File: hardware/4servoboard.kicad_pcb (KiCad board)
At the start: 2 copper layers, 22.9 x 23.6 mm, 34 parts, among them J1 USB_C_Receptacle, J2 PWM, J3 UART, J4 GND, J5 V_SERVO, J6 POWER, J7 DEBUG, U1 CH32X035F7P6, U2 XC6206P332MR

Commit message: wip: Rev0.4への更新
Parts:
- removed D1: SERVO_PWR, LED_SMD:LED_0603_1608Metric_Pad1.05x0.95mm_HandSolder
- removed QR*****: qr-uart-fscb, qr:qr-uart-fscb
- removed R11: 5.1k, Resistor_SMD:R_0603_1608Metric_Pad0.98x0.95mm_HandSolder
- removed R5: 1k, Resistor_SMD:R_0603_1608Metric_Pad0.98x0.95mm_HandSolder
- added D3: MCU_LED2, LED_SMD:LED_0603_1608Metric_Pad1.05x0.95mm_HandSolder, F.Cu at (127.9, 57.0)
- added J8: DEBUG, Connector_PinHeader_2.54mm:PinHeader_1x02_P2.54mm_Vertical, F.Cu at (127.4, 59.5)
- added R17: 5k1, Resistor_SMD:R_0603_1608Metric_Pad0.98x0.95mm_HandSolder, F.Cu at (115.7, 59.4)
- added REF**: MountingHole_2.2mm_M2_DIN965_Pad, MountingHole:MountingHole_2.2mm_M2_DIN965_Pad, F.Cu at (122.3, 54.4)
- added REF**: MountingHole_2.2mm_M2_DIN965_Pad, MountingHole:MountingHole_2.2mm_M2_DIN965_Pad, F.Cu at (130.7, 54.4)
- D2: value MCU_LED -> MCU_LED1
- J1: footprint PCM_SparkFun-Connector:USB-C_16 -> Download_Lib:USB-C_16-HandSolder
- J6: value POWER -> VBUS; footprint Connector_PinHeader_2.54mm:PinHeader_1x04_P2.54mm_Vertical -> Connector_PinHeader_2.54mm:PinHeader_1x02_P2.54mm_Vertical
- J7: value DEBUG -> GND; footprint Connector_PinHeader_1.27mm:PinHeader_1x02_P1.27mm_Vertical -> Connector_PinHeader_2.54mm:PinHeader_1x02_P2.54mm_Vertical
- R10: value 120k -> 1k
- R12, R13: value 1k -> 5k1
- R14, R8: value 5.1k -> 5k1
- R15, R16: value 1k -> 22
- TH1: value Thermistor_NTC -> 22k/B4050/NTC; footprint Resistor_SMD:R_0603_1608Metric_Pad0.98x0.95mm_HandSolder -> PCM_Resistor_SMD_AKL:R_0603_1608Metric_Pad0.98x0.95mm_HandSolder
- U2: footprint Package_TO_SOT_SMD:SOT-23_Handsoldering -> Package_TO_SOT_SMD:SOT-23
- moved D2 111.6 mm to (116.7, 57.0), turned to 0 degrees
- moved R15 108.7 mm to (117.4, 59.4), turned to -90 degrees
- moved R13 106.2 mm to (118.9, 59.4), turned to 90 degrees
- moved R8 106.0 mm to (115.7, 62.7), turned to 90 degrees
- moved R7 106.0 mm to (115.7, 66.0), turned to 90 degrees
- moved C2 105.8 mm to (119.8, 72.3), turned to 180 degrees
- moved R12 104.8 mm to (120.4, 59.4), turned to 90 degrees
- moved R16 104.0 mm to (121.9, 59.4), turned to -90 degrees
- moved R4 102.8 mm to (115.9, 73.0), turned to 90 degrees
- moved JP1 102.8 mm to (118.1, 60.0), turned to 180 degrees
- moved U2 102.6 mm to (119.5, 69.9), turned to 180 degrees
- moved R3 101.5 mm to (117.3, 73.0), turned to 90 degrees
- moved R14 100.1 mm to (116.8, 69.6)
- moved J7 99.9 mm to (128.8, 73.2)
- moved R6 99.7 mm to (120.0, 57.0)
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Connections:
- net PWM2 renamed PWM2/ADC2
- J2 pad 1: PWM0 -> PWM0/ADC0
- J2 pad 2: PWM1 -> PWM1/ADC1
- J2 pad 4: PWM3 -> PWM3/ADC3
- J6 pad 2: GND -> VBUS
- J7 pad 1: SWCLK -> GND
- J7 pad 2: SWDIO -> GND
- JP1 pad 1: DP -> Net-(JP1-A)
- R10 pad 1: OPA_O -> VDD
- R10 pad 2: OPA_N -> Net-(D3-K)
- R14 pad 2: PC3 -> TEMP_SENCE
- R15 pad 2: TX2 -> UART_B
- R16 pad 2: TX4 -> UART_A
- R6 pad 2: MCU_LED -> MCU_LED1
- R7 pad 2: PB1 -> V_SENCE
- R8 pad 1: PB1 -> V_SENCE
- TH1 pad 1: PC3 -> TEMP_SENCE
- U1 pad 1: PWM0 -> MCU_LED1
- U1 pad 10: OPA_O -> unconnected-(U1-PA4-Pad10)
- U1 pad 11: TX4 -> UART_B
- U1 pad 12: MCU_LED -> V_SENCE
- U1 pad 14: PB1 -> TEMP_SENCE
- U1 pad 4: PC3 -> MCU_LED2
- U1 pad 5: PWM1 -> PWM3/ADC3
- U1 pad 7: OPA_N -> PWM1/ADC1
- U1 pad 8: TX2 -> UART_A
- U1 pad 9: PWM3 -> PWM0/ADC0
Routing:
- net GND: track 154.2 -> 28.4 mm, vias 17 -> 24
- net VBUS: track 119.0 -> 22.5 mm, vias 10 -> 5
- net PC3: track 22.8 -> 0.00 mm, vias 2 -> 0
- net CC1: track 37.3 -> 15.1 mm, vias 3 -> 0
- net TEMP_SENCE: track 0.00 -> 19.7 mm, vias 0 -> 4
- net Net-(J1-D--PadA7): track 28.5 -> 12.6 mm
- net MCU_LED: track 15.9 -> 0.00 mm, vias 2 -> 0
- net PWM3: track 15.9 -> 0.00 mm, vias 1 -> 0
- net PWM1: track 15.7 -> 0.00 mm, vias 1 -> 0
- net Net-(J1-D+-PadA6): track 27.4 -> 11.8 mm
- net TX2: track 15.3 -> 0.00 mm, vias 4 -> 0
- net PWM2/ADC2: track 20.3 -> 5.26 mm, vias 1 -> 0
- net MCU_LED2: track 0.00 -> 14.4 mm, vias 0 -> 2
- net PB1: track 14.2 -> 0.00 mm, vias 2 -> 0
- net TX4: track 13.5 -> 0.00 mm, vias 2 -> 0
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- added copper zone on B.Cu, net OPA_P
- added copper zone on F.Cu, net OPA_P
- added copper zone on B.Cu, net VBUS
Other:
- board size 22.9 x 23.6 mm -> 18.7 x 32.9 mm
- board text removed: "DLM(4.7k)"
- board text removed: "GND"
- board text removed: "Made by EsEhEhElp"
- board text removed: "PWM"
- board text removed: "SWCLK"
- board text removed: "SWDIO"
- board text removed: "UART-FSCB V0.3"
- board text removed: "UART0"
- board text removed: "UART1"
- board text removed: "VBUS"

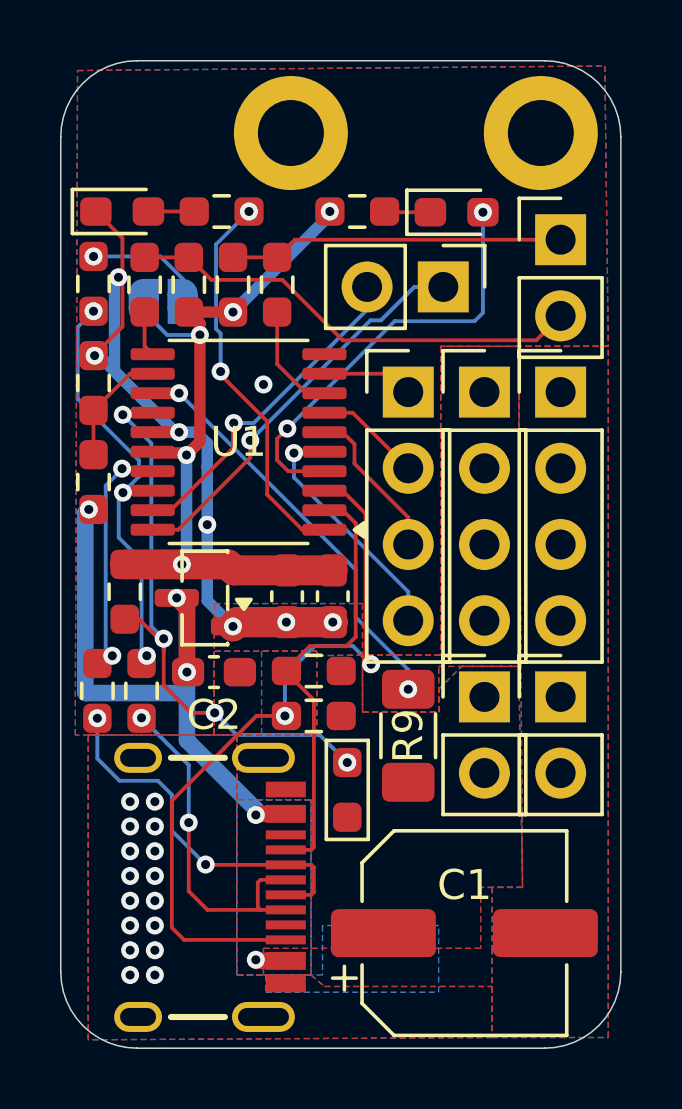
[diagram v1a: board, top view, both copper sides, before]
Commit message: feat: V0.4移行、電源回路の強化
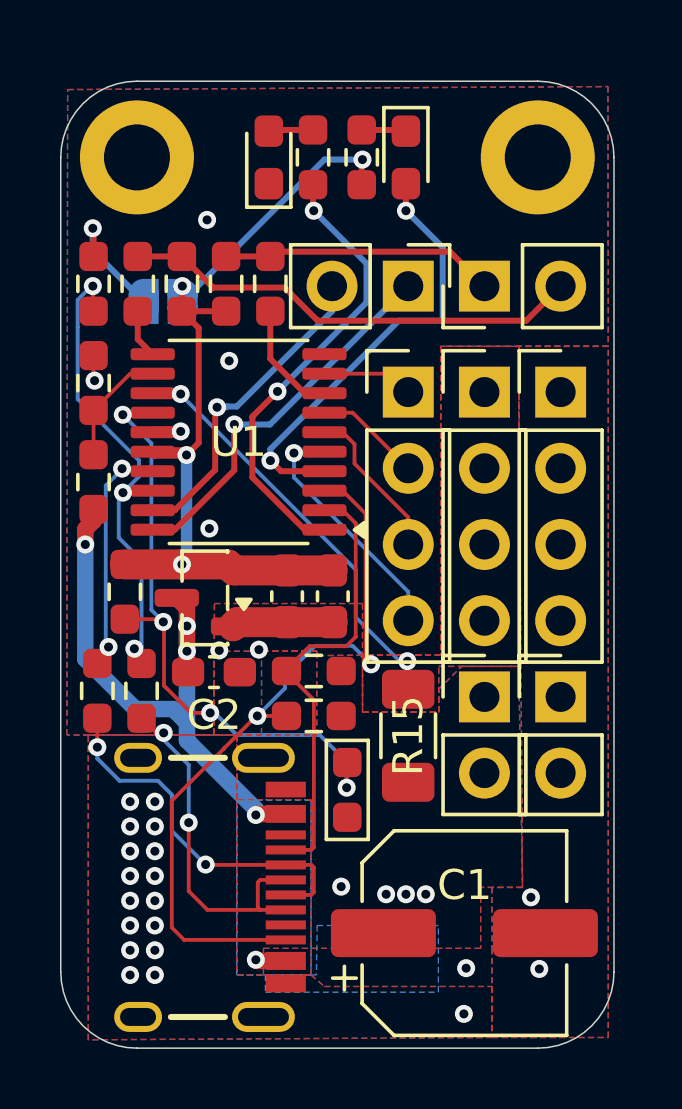
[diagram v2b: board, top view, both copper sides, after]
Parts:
- removed R16: 22, Resistor_SMD:R_0603_1608Metric_Pad0.98x0.95mm_HandSolder
- removed R17: 5k1, Resistor_SMD:R_0603_1608Metric_Pad0.98x0.95mm_HandSolder
- added R12: 22, Resistor_SMD:R_0603_1608Metric_Pad0.98x0.95mm_HandSolder, F.Cu at (121.6, 59.4)
- added R9: 5k1, Resistor_SMD:R_0603_1608Metric_Pad0.98x0.95mm_HandSolder, F.Cu at (115.7, 59.4)
- moved D2 5.21 mm to (121.6, 55.2), turned to 90 degrees
- moved REF2 5.20 mm to (117.2, 55.2)
- moved R5 3.54 mm to (123.1, 55.2), turned to -90 degrees
- moved J3 2.98 mm to (128.8, 59.5), turned to 90 degrees
- moved D3 2.49 mm to (126.2, 55.2), turned to -90 degrees
- moved R6 1.81 mm to (124.7, 55.2), turned to 90 degrees
- moved J8 1.17 mm to (126.2, 59.5)
- moved REF1 0.82 mm to (130.6, 55.2)
- moved R11 0.23 mm to (117.2, 59.4)
- moved R13 0.23 mm to (120.2, 59.4)
- moved R14 0.23 mm to (118.7, 59.4)
- turned JP1 to 0 degrees
- renumbered R14 to R10, R15 to R11, R12 to R13, R13 to R14, R9 to R15, R6 to R5, R10 to R6, REF** to REF1, REF** to REF2
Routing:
- net GND: track 28.4 -> 5.28 mm, vias 24 -> 28
- net VDD: track 25.7 -> 28.7 mm, vias 5 -> 4
- net MCU_LED1: track 13.0 -> 15.2 mm
- net Net-(J3-Pin_1): track 11.2 -> 9.15 mm
- net DP: track 14.2 -> 15.8 mm
- net VBUS: track 22.5 -> 21.3 mm, vias 5 -> 8
- net TEMP_SENCE: track 19.7 -> 20.8 mm
- net SWCLK: track 13.4 -> 12.8 mm
- net MCU_LED2: track 14.4 -> 14.9 mm
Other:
- board size 18.7 x 32.9 mm -> 18.4 x 32.2 mm
- board text added: "A"
- board text added: "B"
- board text added: "G"
- board text added: "GND"
- board text added: "S"
- board text added: "SWC"
- board text added: "SWD"
- board text added: "UART-FSCB V0.4"
- board text added: "V"
- board text added: "VBUS"

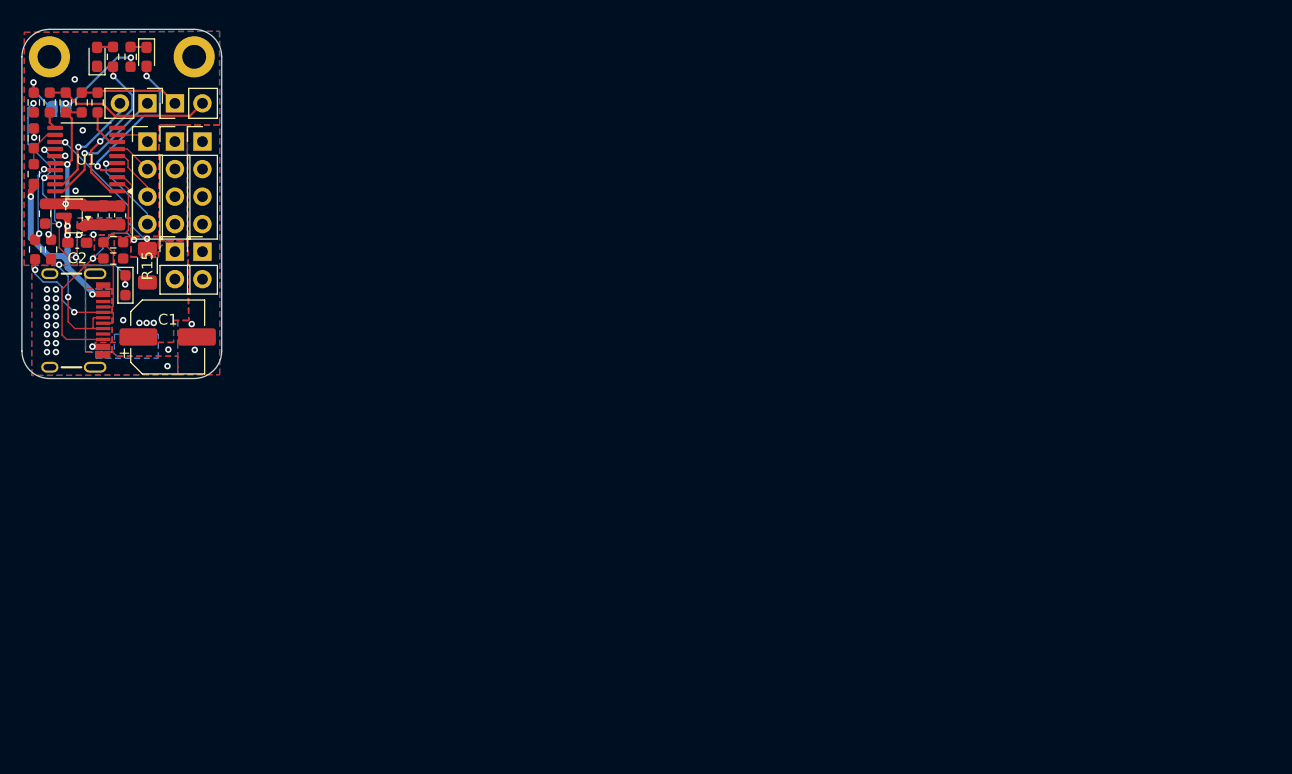
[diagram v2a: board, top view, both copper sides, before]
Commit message: Update: V0.6移行に伴い，四層基板ヘ移行．エラッタ修正，Pch逆接保護回路追加，5.08端子追加
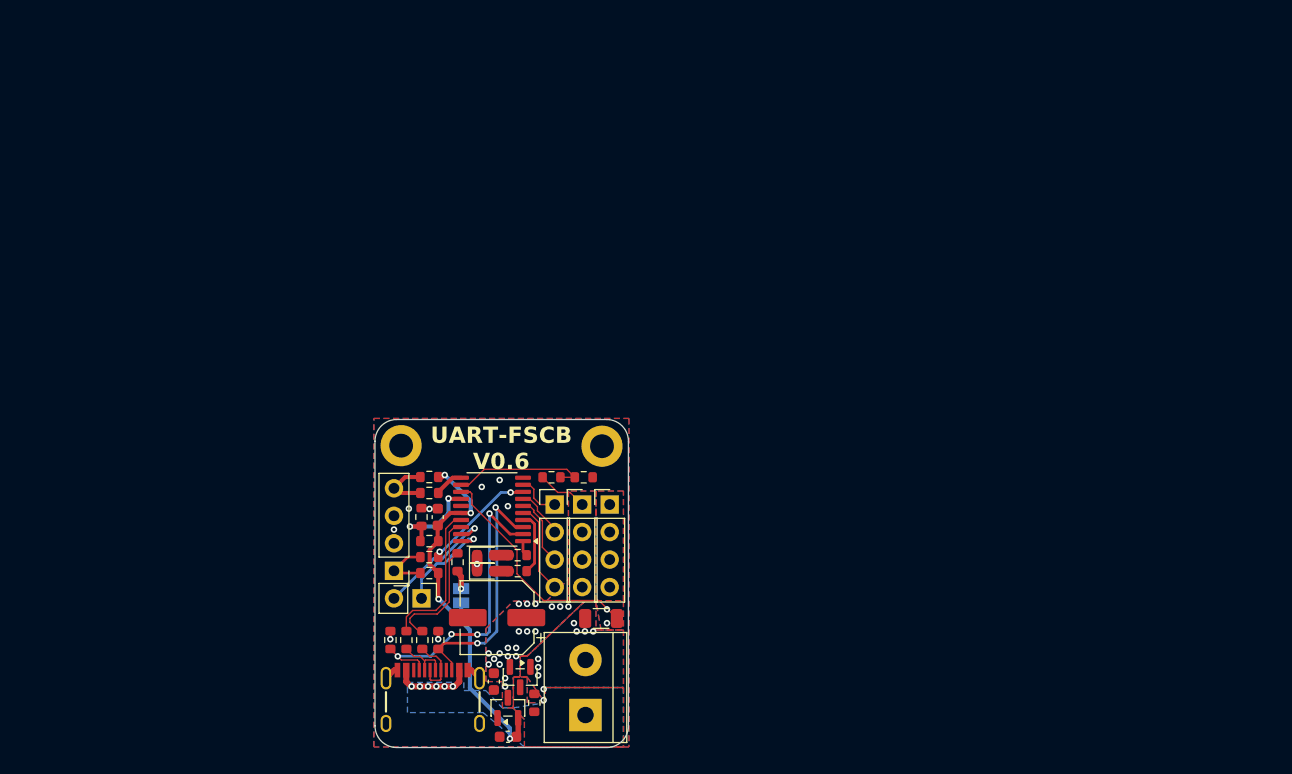
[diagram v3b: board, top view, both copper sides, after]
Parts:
- removed D3: MCU_LED2, LED_SMD:LED_0603_1608Metric_Pad1.05x0.95mm_HandSolder
- removed J8: DEBUG, Connector_PinHeader_2.54mm:PinHeader_1x02_P2.54mm_Vertical
- removed REF1, REF2: MountingHole_2.2mm_M2_DIN965_Pad, MountingHole:MountingHole_2.2mm_M2_DIN965_Pad
- added D1: Red_1.7V, LED_SMD:LED_0603_1608Metric, F.Cu at (157.5, 102.6)
- added Q1: AO3407A, Package_TO_SOT_SMD:SOT-23, F.Cu at (160.6, 112.4)
- added R16: 120k, Resistor_SMD:R_0603_1608Metric, F.Cu at (161.9, 114.8)
- added REF**: MountingHole_2.2mm_M2_DIN965_Pad, MountingHole:MountingHole_2.2mm_M2_DIN965_Pad, F.Cu at (168.2, 91.1)
- added REF**: MountingHole_2.2mm_M2_DIN965_Pad, MountingHole:MountingHole_2.2mm_M2_DIN965_Pad, F.Cu at (149.7, 91.1)
- C1: value 100u/35V -> 220uF/16V
- C2, C3, C4: footprint Capacitor_SMD:C_0603_1608Metric_Pad1.08x0.95mm_HandSolder -> Capacitor_SMD:C_0603_1608Metric
- D2: value MCU_LED1 -> Red_1.7V; footprint LED_SMD:LED_0603_1608Metric_Pad1.05x0.95mm_HandSolder -> LED_SMD:LED_0603_1608Metric
- J2: value PWM -> UART
- J3: value UART -> PWM; footprint Connector_PinHeader_2.54mm:PinHeader_1x02_P2.54mm_Vertical -> Connector_PinHeader_2.54mm:PinHeader_1x04_P2.54mm_Vertical
- J4: value GND -> V_SERVO
- J5: value V_SERVO -> GND
- J6: value VBUS -> EXT_POWER; footprint Connector_PinHeader_2.54mm:PinHeader_1x02_P2.54mm_Vertical -> TerminalBlock:TerminalBlock_bornier-2_P5.08mm
- J7: value GND -> DEBUG
- JP1: value SolderJumper_2_Open -> DLM_JMP; footprint Jumper:SolderJumper-2_P1.3mm_Open_RoundedPad1.0x1.5mm -> Jumper:SolderJumper-2_P1.3mm_Open_Pad1.0x1.5mm
- R1, R2: value 5.1k -> 22; footprint Resistor_SMD:R_0603_1608Metric_Pad0.98x0.95mm_HandSolder -> Resistor_SMD:R_0603_1608Metric
- R10, R7, R8, R9: footprint Resistor_SMD:R_0603_1608Metric_Pad0.98x0.95mm_HandSolder -> Resistor_SMD:R_0603_1608Metric
- R11, R12: value 22 -> 1k; footprint Resistor_SMD:R_0603_1608Metric_Pad0.98x0.95mm_HandSolder -> Resistor_SMD:R_0603_1608Metric
- R13, R14: value 5k1 -> 22; footprint Resistor_SMD:R_0603_1608Metric_Pad0.98x0.95mm_HandSolder -> Resistor_SMD:R_0603_1608Metric
- R15: value 0.02 -> 0.01; footprint Resistor_SMD:R_1206_3216Metric_Pad1.30x1.75mm_HandSolder -> Resistor_SMD:R_1206_3216Metric
- R3, R4: value 22 -> 5.1k; footprint Resistor_SMD:R_0603_1608Metric_Pad0.98x0.95mm_HandSolder -> Resistor_SMD:R_0603_1608Metric
- R5, R6: value 1k -> 2k2; footprint Resistor_SMD:R_0603_1608Metric_Pad0.98x0.95mm_HandSolder -> Resistor_SMD:R_0603_1608Metric
- TH1: footprint PCM_Resistor_SMD_AKL:R_0603_1608Metric_Pad0.98x0.95mm_HandSolder -> Resistor_SMD:R_0603_1608Metric
- U2: value XC6206P332MR -> ME6209A33M3G
- moved U2 60.6 mm to (159.5, 115.3), turned to 90 degrees
- moved R5 60.4 mm to (160.4, 102.6), turned to 0 degrees
- moved C3 60.0 mm to (159.5, 117.9), turned to 180 degrees
- moved R8 59.6 mm to (166.5, 94.0), turned to 0 degrees
- moved D2 58.3 mm to (157.5, 101.2), turned to 0 degrees
- moved JP1 58.3 mm to (155.2, 104.9), turned to -90 degrees
- moved R6 58.2 mm to (160.4, 101.2), turned to 0 degrees
- moved R9 57.7 mm to (154.9, 101.8), turned to 90 degrees
- moved C2 55.9 mm to (158.2, 112.8), turned to 90 degrees
- moved R11 55.8 mm to (152.3, 102.8), turned to 180 degrees
- moved J6 55.5 mm to (166.7, 115.9), turned to 90 degrees
- moved R7 55.4 mm to (163.5, 94.0), turned to 0 degrees
- moved R15 53.0 mm to (168.1, 107.0), turned to 180 degrees
- moved R13 52.8 mm to (152.3, 101.3), turned to 0 degrees
- moved R4 51.8 mm to (153.1, 109.0), turned to -90 degrees
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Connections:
- net TEMP_SENCE renamed TEMP_SENSE
- net V_SENCE renamed V_SENSE
- C1 pad 1: GND -> V_SERVO
- C1 pad 2: VBUS -> GND
- C2 pad 2: VBUS -> V_SERVO
- J2 pad 1: PWM0/ADC0 -> Net-(J2-Pin_1)
- J2 pad 2: PWM1/ADC1 -> GND
- J2 pad 3: PWM2/ADC2 -> GND
- J2 pad 4: PWM3/ADC3 -> Net-(J2-Pin_4)
- J3 pad 1: Net-(J3-Pin_1) -> PWM0/ADC0
- J3 pad 2: Net-(J3-Pin_2) -> PWM1/ADC1
- J4 pad 1: OPA_P -> V_SERVO
- J4 pad 2: OPA_P -> V_SERVO
- J4 pad 3: OPA_P -> V_SERVO
- J4 pad 4: OPA_P -> V_SERVO
- J5 pad 1: VBUS -> CURRENT_SENSE
- J5 pad 2: VBUS -> CURRENT_SENSE
- J5 pad 3: VBUS -> CURRENT_SENSE
- J5 pad 4: VBUS -> CURRENT_SENSE
- J6 pad 2: VBUS -> GND
- J7 pad 1: GND -> SWCLK
- J7 pad 2: GND -> SWDIO
- R1 pad 1: GND -> Net-(J1-D+-PadA6)
- R1 pad 2: CC1 -> D+
- R11 pad 1: Net-(J3-Pin_2) -> VDD
- R11 pad 2: UART_B -> Net-(J2-Pin_1)
- R12 pad 1: Net-(J3-Pin_1) -> VDD
- R12 pad 2: UART_A -> Net-(J2-Pin_4)
- R13 pad 1: VDD -> Net-(J2-Pin_1)
- R13 pad 2: Net-(J3-Pin_1) -> UART_A
- R14 pad 1: VDD -> Net-(J2-Pin_4)
- R14 pad 2: Net-(J3-Pin_2) -> UART_B
- R15 pad 1: OPA_P -> CURRENT_SENSE
- R2 pad 1: GND -> Net-(J1-D--PadA7)
- R2 pad 2: CC2 -> D-
- R3 pad 1: Net-(J1-D+-PadA6) -> GND
- R3 pad 2: DP -> CC1
- R4 pad 1: Net-(J1-D--PadA7) -> GND
- R4 pad 2: DM -> CC2
- R5 pad 1: Net-(D2-A) -> Net-(D1-A)
- R5 pad 2: MCU_LED1 -> MCU_LED2
- R6 pad 1: VDD -> Net-(D2-A)
- R6 pad 2: Net-(D3-K) -> MCU_LED1
- R7 pad 1: VBUS -> V_SERVO
- R9 pad 2: DP -> D+
- U1 pad 13: OPA_P -> CURRENT_SENSE
- U1 pad 17: DM -> D-
- U1 pad 18: DP -> D+
- U2 pad 3: VBUS -> V_SERVO
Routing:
- net CURRENT_SENSE: track 0.00 -> 21.1 mm, vias 0 -> 2
- net DP: track 15.8 -> 0.00 mm, vias 3 -> 0
- net Net-(J3-Pin_2): track 15.5 -> 0.00 mm
- net D+: track 0.00 -> 14.9 mm
- net OPA_P: track 14.6 -> 0.00 mm, vias 2 -> 0
- net D-: track 0.00 -> 14.0 mm
- net VBUS: track 21.3 -> 7.40 mm, vias 8 -> 6
- net MCU_LED1: track 15.2 -> 1.43 mm, vias 2 -> 0
- net CC1: track 15.1 -> 28.2 mm, vias 0 -> 4
- net TEMP_SENSE: track 20.8 -> 9.14 mm, vias 4 -> 2
- net Net-(J3-Pin_1): track 9.15 -> 0.00 mm
- net MCU_LED2: track 14.9 -> 5.87 mm, vias 2 -> 0
- net V_SENSE: track 3.95 -> 12.7 mm
- net Net-(J1-D--PadA7): track 12.6 -> 4.91 mm, vias 2 -> 0
- net VDD: track 28.7 -> 36.1 mm
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- added copper zone on B.Cu, net CURRENT_SENSE
- added copper zone on F.Cu, net CURRENT_SENSE
- added copper zone on In1.Cu, net CURRENT_SENSE
- added copper zone on In2.Cu, net CURRENT_SENSE
- added copper zone on In1.Cu, net GND
- added copper zone on In2.Cu, net GND
- added copper zone on In1.Cu, net VBUS
- added copper zone on In2.Cu, net VBUS
- added copper zone on B.Cu, net V_SERVO
- added copper zone on F.Cu, net V_SERVO
- added copper zone on In1.Cu, net V_SERVO
- added copper zone on In2.Cu, net V_SERVO
- removed copper zone on B.Cu, net OPA_P
- removed copper zone on F.Cu, net OPA_P
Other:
- board size 18.4 x 32.2 mm -> 23.4 x 30.3 mm
- copper layers 2 -> 4
- board text added: "+"
- board text added: "-"
- board text added: "DLM"
- board text added: "S V G"
- board text added: "UART-FSCB V0.6"
- board text added: "UART_B GND GND UART_A"
- board text removed: "A"
- board text removed: "B"
- board text removed: "G"
- board text removed: "GND"
- board text removed: "S"
- board text removed: "SWC"
- board text removed: "SWD"
- board text removed: "UART-FSCB V0.4"
- board text removed: "V"
- board text removed: "VBUS"

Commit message: Fix: 基板デザインの効率化が主．内容：アートワークの最適化，viaの追加など
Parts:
- R5, R6: value 2k2 -> 1k
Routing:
- net V_SERVO: vias 20 -> 21
- net VBUS: vias 6 -> 12
- net GND: vias 18 -> 20
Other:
- outline, holes or cut-outs redrawn
- board text removed: "-"
